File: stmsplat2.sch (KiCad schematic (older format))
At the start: 102 parts, among them J1 C11_2X36, J10 Conn_01x03_Male, J11 Conn_01x02_Male, J12 Conn_01x04_Male, J13 Conn_01x04_Male, J14 Conn_01x02, J15 Conn_01x02, J16 Screw_Terminal_01x03, J17 Screw_Terminal_01x02, J2 C12_2X36, J3 Conn_01x04_Male, J4 Conn_01x04_Male, J5 Conn_Coaxial, J6 Conn_01x04_Male, J7 Conn_01x04_Male, J8 Conn_01x04_Male, J9 Conn_01x03_Male, Q1 BSS138LT1G, U1 ublox_chinese_PCB_module, U10 XCVR_E30-400M20S, U11 3115_module, U2 ESP-C3-13U, U3 SST25VF032B, U4 48L512-48LM01, U5 Opamp_Quad_MCP6024, U6 E180-ZG120A, U7 AZ1084C, U8 MCP6S93-X_UN, U9 DS2485

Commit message: Added a few passives in sch. Library update may not be good? Placement tweaks.
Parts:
- added C27: 0.1uF, Capacitor_SMD:C_0805_2012Metric_Pad1.15x1.40mm_HandSolder, symbol Device:C
- added C28: 100uF, Capacitor_SMD:CP_Elec_8x10, symbol Device:CP
- added R21, R22: 4K7, Resistor_SMD:R_0805_2012Metric, symbol Device:R
- C18, C22, C3: footprint Capacitor_SMD:C_0402_1005Metric -> Capacitor_SMD:C_0805_2012Metric
- C26: footprint Capacitor_SMD:C_0603_1608Metric -> Capacitor_SMD:C_0805_2012Metric
- U10: value XCVR_E30-400M20S -> XCVR_E30-400M20S (Si4463); Version (none) -> The module with the Si4463 (not Si4438) is prefered
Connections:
- net GND: now also C27.1, C28.2
- net PB5: now also R22.2
- net PE15: now also R21.2
- net PE8: now also C27.2
- net VDD: now also C28.1, R21.1, R22.1
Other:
- note added: "VER 0.10: FROZEN"
- note removed: "VER 0.09: ALMOST FROZEN \n"
- moved on the sheet: C1, C2, C3
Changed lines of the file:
@@
 Text GLabel 1200 5300 0    50   Input ~ 0
 PF9
-Text GLabel 6750 6400 2    50   Input ~ 0
+Text GLabel 7350 6400 2    50   Input ~ 0
 PE15
 $Comp
@@
 L Device:C C3
 U 1 1 5BDACAE4
-P 2500 10050
-F 0 "C3" H 2618 10096 50  0000 L CNN
-F 1 "1uF" H 2618 10005 50  0000 L CNN
-F 2 "Capacitor_SMD:C_0402_1005Metric" H 2538 9900 50  0001 C CNN
-F 3 "~" H 2500 10050 50  0001 C CNN
-	1    2500 10050
+P 2250 10050
+F 0 "C3" H 2368 10096 50  0000 L CNN
+F 1 "1uF" H 2368 10005 50  0000 L CNN
+F 2 "Capacitor_SMD:C_0805_2012Metric" H 2288 9900 50  0001 C CNN
+F 3 "~" H 2250 10050 50  0001 C CNN
+	1    2250 10050
 	1    0    0    -1
 $EndComp
@@
 	3650 9600 3650 9250
 Wire Wire Line
-	2500 9900 2500 9250
+	2250 9900 2250 9250
 Wire Wire Line
-	2500 10200 2500 10900
+	2250 10200 2250 10900
 Wire Wire Line
 	3750 10900 3750 10600
@@
 P 14300 5350
 F 0 "U10" H 14350 6515 50  0000 C CNN
-F 1 "XCVR_E30-400M20S" H 14350 6424 50  0000 C CNN
+F 1 "XCVR_E30-400M20S (Si4463)" H 14350 6424 50  0000 C CNN
 F 2 "XCVR_E30-400M20S" H 14300 4100 50  0001 C CNN
-F 3 "" H 14450 4100 50  0001 C CNN
+F 3 "https://www.aliexpress.com/item/1005003341113107.html?spm=a2g0o.productlist.0.0.33ec1646kOjmw0&algo_pvid=cdcf01bc-679d-405a-bcd6-5e089ec52c01&algo_exp_id=cdcf01bc-679d-405a-bcd6-5e089ec52c01-11&pdp_ext_f=%7B%22sku_id%22%3A%2212000025304774495%22%7D" H 14450 4100 50  0001 C CNN
+F 4 "The module with the Si4463 (not Si4438) is prefered" H 14300 5350 50  0001 C CNN "Version"
 	1    14300 5350
 	1    0    0    -1
@@
 	3800 7950 3950 7950
 Wire Wire Line
-	6650 6400 6750 6400
+	6650 6400 6700 6400
 Text GLabel 5350 3100 0    50   Input ~ 0
 PC10
@@
 Wire Wire Line
 	7200 7350 7750 7350
-Text GLabel 9800 4500 0    50   Input ~ 0
-PE8
 Text GLabel 1650 1000 2    50   Input ~ 0
 PC11
@@
 	1    0    0    -1
 $EndComp
-Connection ~ 2500 9250
-Connection ~ 2500 10900
-Wire Wire Line
-	2500 10900 3400 10900
 Text GLabel 6800 9700 0    50   Input ~ 0
 PA4
@@
 Connection ~ 1000 10150
 Wire Wire Line
-	2850 10700 2850 10100
+	3000 10700 3000 10100
 Connection ~ 1000 10300
-Wire Wire Line
-	2500 9250 3650 9250
 $Comp
 L stmsplat2-custom:ublox_SAM-M8Q U1
@@
 $EndComp
 Wire Wire Line
-	2850 10100 3250 10100
+	3000 10100 3250 10100
 Wire Wire Line
 	6650 7300 7150 7300
@@
 L Device:CP C2
 U 1 1 64F25216
-P 1950 10050
-F 0 "C2" H 2068 10096 50  0000 L CNN
-F 1 "10uF" H 2068 10005 50  0000 L CNN
-F 2 "Capacitor_THT:CP_Radial_D5.0mm_P2.50mm" H 1988 9900 50  0001 C CNN
-F 3 "~" H 1950 10050 50  0001 C CNN
-	1    1950 10050
+P 1800 10050
+F 0 "C2" H 1918 10096 50  0000 L CNN
+F 1 "10uF" H 1918 10005 50  0000 L CNN
+F 2 "Capacitor_THT:CP_Radial_D5.0mm_P2.50mm" H 1838 9900 50  0001 C CNN
+F 3 "~" H 1800 10050 50  0001 C CNN
+	1    1800 10050
 	1    0    0    -1
 $EndComp
 Wire Wire Line
-	1950 9250 1950 9900
-Connection ~ 1950 9250
-Wire Wire Line
-	1950 9250 2500 9250
+	1800 9250 1800 9900
 $Comp
 L Device:C C1
 U 1 1 65067AB3
-P 1450 10050
-F 0 "C1" H 1565 10096 50  0000 L CNN
-F 1 "0.1uF" H 1565 10005 50  0000 L CNN
-F 2 "Capacitor_SMD:C_0805_2012Metric" H 1488 9900 50  0001 C CNN
-F 3 "~" H 1450 10050 50  0001 C CNN
-	1    1450 10050
+P 1350 10050
+F 0 "C1" H 1465 10096 50  0000 L CNN
+F 1 "0.1uF" H 1465 10005 50  0000 L CNN
+F 2 "Capacitor_SMD:C_0805_2012Metric" H 1388 9900 50  0001 C CNN
+F 3 "~" H 1350 10050 50  0001 C CNN
+	1    1350 10050
 	1    0    0    -1
 $EndComp
 Wire Wire Line
-	1450 9250 1450 9900
-Connection ~ 1450 9250
-Wire Wire Line
-	1450 9250 1950 9250
-Wire Wire Line
-	1300 10900 1450 10900
-Wire Wire Line
-	1450 10200 1450 10900
-Connection ~ 1450 10900
+	1350 9250 1350 9900
 Wire Wire Line
-	1450 10900 1950 10900
+	1300 10900 1350 10900
 Wire Wire Line
-	1950 10200 1950 10900
-Connection ~ 1950 10900
+	1350 10200 1350 10900
 Wire Wire Line
-	1950 10900 2500 10900
+	1800 10200 1800 10900
 Wire Wire Line
-	1000 10700 2850 10700
+	1000 10700 3000 10700
 $Comp
 L power:GND #PWR05
@@
 Text Notes 8800 5200 0    50   ~ 0
 STM UART4
-Wire Wire Line
-	9800 4500 9950 4500
 Text GLabel 12150 5600 2    50   Input ~ 0
 PG0
@@
 Wire Wire Line
 	9400 3750 10200 3750
-Wire Wire Line
-	10200 3950 9900 3950
 $Comp
 L power:GND #PWR04
 U 1 1 65959B83
-P 9900 4200
-F 0 "#PWR04" H 9900 3950 50  0001 C CNN
-F 1 "GND" H 9905 4027 50  0000 C CNN
-F 2 "" H 9900 4200 50  0001 C CNN
-F 3 "" H 9900 4200 50  0001 C CNN
-	1    9900 4200
+P 9600 4200
+F 0 "#PWR04" H 9600 3950 50  0001 C CNN
+F 1 "GND" H 9605 4027 50  0000 C CNN
+F 2 "" H 9600 4200 50  0001 C CNN
+F 3 "" H 9600 4200 50  0001 C CNN
+	1    9600 4200
 	1    0    0    -1
 $EndComp
 Wire Wire Line
-	9900 3950 9900 4200
+	9600 3950 9600 4200
 Text GLabel 9950 3450 1    50   Input ~ 0
 VDD
@@
 	1    0    0    1
 $EndComp
-Text GLabel 7950 6300 1    50   Input ~ 0
+Text GLabel 8350 5800 2    50   Input ~ 0
 VDD
 Wire Wire Line
@@
 	7100 6950 7550 6950
 Wire Wire Line
-	7950 6300 7950 6550
-Wire Wire Line
 	12050 6600 11950 6600
 Text Label 13000 6300 0    50   ~ 0
@@
 SHUTDOWN
 Wire Wire Line
-	12950 5800 13450 5800
+	12950 5800 13200 5800
 Wire Wire Line
 	15250 5400 15600 5400
@@
 Text Notes 11200 4050 0    89   ~ 0
 ZIGBEE
-Text Notes 13400 4300 0    89   ~ 0
+Text Notes 13750 4150 0    89   ~ 0
 433MHz\n GFSK
 $Comp
@@
 F 0 "C18" H 12818 9146 50  0000 L CNN
 F 1 "1uF" H 12818 9055 50  0000 L CNN
-F 2 "Capacitor_SMD:C_0402_1005Metric" H 12738 8950 50  0001 C CNN
+F 2 "Capacitor_SMD:C_0805_2012Metric" H 12738 8950 50  0001 C CNN
 F 3 "~" H 12700 9100 50  0001 C CNN
 	1    12700 9100
@@
 F 0 "C22" H 14000 9100 50  0000 L CNN
 F 1 "1uF" H 14000 8850 50  0000 L CNN
-F 2 "Capacitor_SMD:C_0402_1005Metric" H 13988 8800 50  0001 C CNN
+F 2 "Capacitor_SMD:C_0805_2012Metric" H 13988 8800 50  0001 C CNN
 F 3 "~" H 13950 8950 50  0001 C CNN
 	1    13950 8950
@@
 Connection ~ 1000 9250
 Wire Wire Line
-	1000 9250 1450 9250
+	1000 9250 1350 9250
 $Comp
 L Device:C C10
@@
 SERIAL FLASH ROM\n  AND NVRAM
 Text Notes 11900 10500 0    89   Italic 0
-VER 0.09: ALMOST FROZEN \n
+VER 0.10: FROZEN
 $Comp
 L Connector_Generic:Conn_01x02 J14
@@
 F 0 "C26" H 14750 9100 50  0000 L CNN
 F 1 "0.1uF" H 14750 8850 50  0000 L CNN
-F 2 "Capacitor_SMD:C_0603_1608Metric" H 14738 8800 50  0001 C CNN
+F 2 "Capacitor_SMD:C_0805_2012Metric" H 14738 8800 50  0001 C CNN
 F 3 "~" H 14700 8950 50  0001 C CNN
 	1    14700 8950
@@
 Wire Wire Line
 	14000 900  15500 900
+$Comp
+L Device:R R21
+U 1 1 61AD7259
+P 7450 6050
+F 0 "R21" H 7520 6096 50  0000 L CNN
+F 1 "4K7" H 7520 6005 50  0000 L CNN
+F 2 "Resistor_SMD:R_0805_2012Metric" V 7380 6050 50  0001 C CNN
+F 3 "~" H 7450 6050 50  0001 C CNN
+	1    7450 6050
+	1    0    0    -1
+$EndComp
+Wire Wire Line
+	7450 6200 6700 6200
+Wire Wire Line
+	6700 6200 6700 6400
+Connection ~ 6700 6400
+Wire Wire Line
+	6700 6400 7350 6400
+Wire Wire Line
+	7450 5900 7450 5800
+Wire Wire Line
+	7450 5800 7950 5800
+Wire Wire Line
+	7950 5800 7950 6550
+Connection ~ 7950 5800
+Wire Wire Line
+	7950 5800 8350 5800
+$Comp
+L Device:C C27
+U 1 1 61C35F32
+P 9900 4250
+F 0 "C27" H 10015 4296 50  0000 L CNN
+F 1 "0.1uF" H 9700 4400 50  0000 L CNN
+F 2 "Capacitor_SMD:C_0805_2012Metric_Pad1.15x1.40mm_HandSolder" H 9938 4100 50  0001 C CNN
+F 3 "~" H 9900 4250 50  0001 C CNN
+	1    9900 4250
+	1    0    0    -1
+$EndComp
+Wire Wire Line
+	10200 3950 9900 3950
+Wire Wire Line
+	9900 4100 9900 3950
+Connection ~ 9900 3950
+Wire Wire Line
+	9900 3950 9600 3950
+Wire Wire Line
+	9900 4400 9900 4500
+Connection ~ 9900 4500
+Wire Wire Line
+	9900 4500 9950 4500
+Text GLabel 9700 4500 0    50   Input ~ 0
+PE8
+Wire Wire Line
+	9700 4500 9900 4500
+$Comp
+L Device:R R22
+U 1 1 61DF47DA
+P 13200 5250
+F 0 "R22" H 13270 5296 50  0000 L CNN
+F 1 "4K7" H 13270 5205 50  0000 L CNN
+F 2 "Resistor_SMD:R_0805_2012Metric" V 13130 5250 50  0001 C CNN
+F 3 "~" H 13200 5250 50  0001 C CNN
+	1    13200 5250
+	1    0    0    -1
+$EndComp
+Wire Wire Line
+	13200 5400 13200 5800
+Connection ~ 13200 5800
+Wire Wire Line
+	13200 5800 13450 5800
+Wire Wire Line
+	12800 4000 13200 4000
+Wire Wire Line
+	13200 4000 13200 5100
+Connection ~ 12800 4000
+$Comp
+L Device:CP C28
+U 1 1 6202CE0B
+P 2650 10050
+F 0 "C28" H 2768 10096 50  0000 L CNN
+F 1 "100uF" H 2768 10005 50  0000 L CNN
+F 2 "Capacitor_SMD:CP_Elec_8x10" H 2688 9900 50  0001 C CNN
+F 3 "~" H 2650 10050 50  0001 C CNN
+	1    2650 10050
+	1    0    0    -1
+$EndComp
+Connection ~ 1350 9250
+Connection ~ 1350 10900
+Wire Wire Line
+	1350 9250 1800 9250
+Wire Wire Line
+	1350 10900 1800 10900
+Connection ~ 1800 9250
+Connection ~ 1800 10900
+Wire Wire Line
+	1800 9250 2250 9250
+Wire Wire Line
+	1800 10900 2250 10900
+Connection ~ 2250 9250
+Connection ~ 2250 10900
+Wire Wire Line
+	2250 9250 2650 9250
+Wire Wire Line
+	2650 9900 2650 9250
+Connection ~ 2650 9250
+Wire Wire Line
+	2650 9250 3650 9250
+Wire Wire Line
+	2650 10200 2650 10900
+Wire Wire Line
+	2250 10900 2650 10900
+Connection ~ 2650 10900
+Wire Wire Line
+	2650 10900 3400 10900
 $EndSCHEMATC

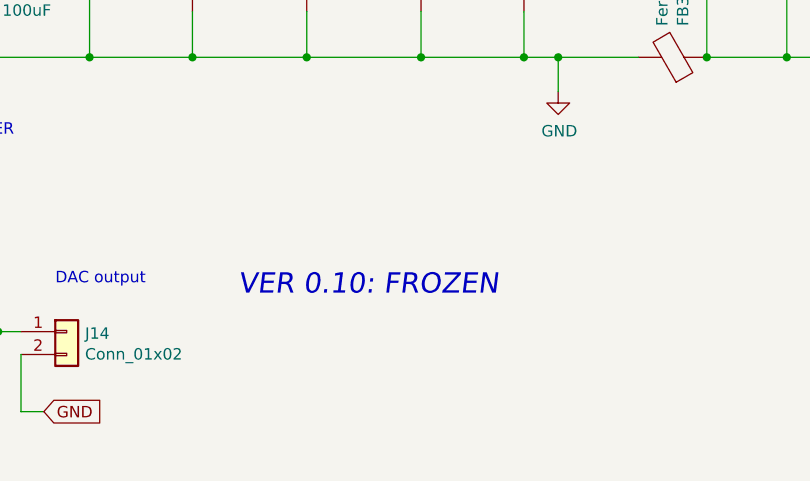
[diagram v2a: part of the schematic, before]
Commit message: Few footprints changes, placement changes, initial routing success
SCH: 0.11 (now feature frozen)
PCB: Placement 1.2
PCB Routed 1.0
The unrouted pcb is also in this folder
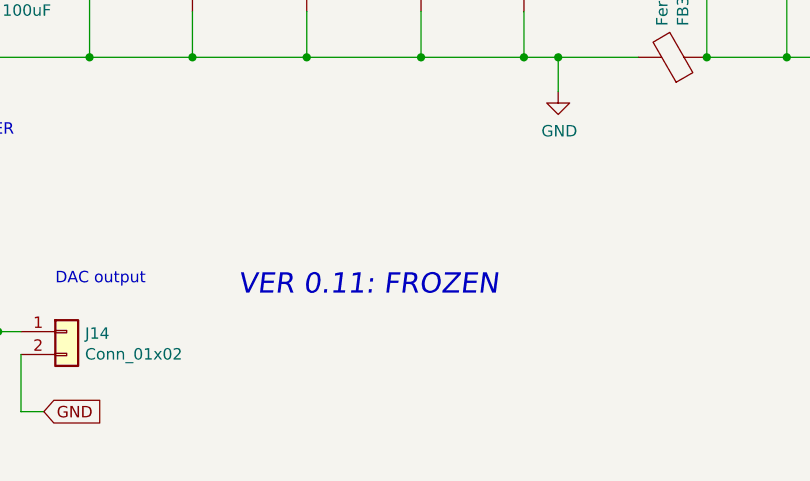
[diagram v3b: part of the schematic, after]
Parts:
- C11, C15, C25, C28: footprint Capacitor_SMD:CP_Elec_8x10 -> Capacitor_SMD:CP_Elec_6.3x7.7
- C2, C23: footprint Capacitor_THT:CP_Radial_D5.0mm_P2.50mm -> Capacitor_SMD:CP_Elec_5x5.4
- C20, C5: footprint Capacitor_THT:CP_Radial_D5.0mm_P2.50mm -> Capacitor_SMD:CP_Elec_6.3x7.7
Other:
- note added: "VER 0.11: FROZEN"
- note removed: "VER 0.10: FROZEN"
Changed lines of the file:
@@
 F 0 "C23" H 14350 9100 50  0000 L CNN
 F 1 "10uF" H 14350 8850 50  0000 L CNN
-F 2 "Capacitor_THT:CP_Radial_D5.0mm_P2.50mm" H 14338 8800 50  0001 C CNN
+F 2 "Capacitor_SMD:CP_Elec_5x5.4" H 14338 8800 50  0001 C CNN
 F 3 "~" H 14300 8950 50  0001 C CNN
 	1    14300 8950
@@
 F 0 "C15" H 12318 9146 50  0000 L CNN
 F 1 "100uF" H 12318 9055 50  0000 L CNN
-F 2 "Capacitor_SMD:CP_Elec_8x10" H 12238 8950 50  0001 C CNN
+F 2 "Capacitor_SMD:CP_Elec_6.3x7.7" H 12238 8950 50  0001 C CNN
 F 3 "~" H 12200 9100 50  0001 C CNN
 	1    12200 9100
@@
 F 0 "C5" V 7100 4250 50  0000 L CNN
 F 1 "100uF" V 7400 4200 50  0000 L CNN
-F 2 "Capacitor_THT:CP_Radial_D5.0mm_P2.50mm" H 7288 4150 50  0001 C CNN
+F 2 "Capacitor_SMD:CP_Elec_6.3x7.7" H 7288 4150 50  0001 C CNN
 F 3 "~" H 7250 4300 50  0001 C CNN
 	1    7250 4300
@@
 F 0 "C2" H 1918 10096 50  0000 L CNN
 F 1 "10uF" H 1918 10005 50  0000 L CNN
-F 2 "Capacitor_THT:CP_Radial_D5.0mm_P2.50mm" H 1838 9900 50  0001 C CNN
+F 2 "Capacitor_SMD:CP_Elec_5x5.4" H 1838 9900 50  0001 C CNN
 F 3 "~" H 1800 10050 50  0001 C CNN
 	1    1800 10050
@@
 F 0 "C20" H 13268 9146 50  0000 L CNN
 F 1 "10uF" H 13268 9055 50  0000 L CNN
-F 2 "Capacitor_THT:CP_Radial_D5.0mm_P2.50mm" H 13188 8950 50  0001 C CNN
+F 2 "Capacitor_SMD:CP_Elec_6.3x7.7" H 13188 8950 50  0001 C CNN
 F 3 "~" H 13150 9100 50  0001 C CNN
 	1    13150 9100
@@
 F 0 "C25" H 15200 9100 50  0000 L CNN
 F 1 "100uF" H 15200 8850 50  0000 L CNN
-F 2 "Capacitor_SMD:CP_Elec_8x10" H 15188 8800 50  0001 C CNN
+F 2 "Capacitor_SMD:CP_Elec_6.3x7.7" H 15188 8800 50  0001 C CNN
 F 3 "~" H 15150 8950 50  0001 C CNN
 	1    15150 8950
@@
 F 0 "C11" H 10868 9246 50  0000 L CNN
 F 1 "100uF" H 10868 9155 50  0000 L CNN
-F 2 "Capacitor_SMD:CP_Elec_8x10" H 10788 9050 50  0001 C CNN
+F 2 "Capacitor_SMD:CP_Elec_6.3x7.7" H 10788 9050 50  0001 C CNN
 F 3 "~" H 10750 9200 50  0001 C CNN
 	1    10750 9200
@@
 SERIAL FLASH ROM\n  AND NVRAM
 Text Notes 11900 10500 0    89   Italic 0
-VER 0.10: FROZEN
+VER 0.11: FROZEN
 $Comp
 L Connector_Generic:Conn_01x02 J14
@@
 F 0 "C28" H 2768 10096 50  0000 L CNN
 F 1 "100uF" H 2768 10005 50  0000 L CNN
-F 2 "Capacitor_SMD:CP_Elec_8x10" H 2688 9900 50  0001 C CNN
+F 2 "Capacitor_SMD:CP_Elec_6.3x7.7" H 2688 9900 50  0001 C CNN
 F 3 "~" H 2650 10050 50  0001 C CNN
 	1    2650 10050
